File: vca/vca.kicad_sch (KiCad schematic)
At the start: 22 parts, among them U4 STM32F103C6Tx, Y1 Crystal_8Mhz

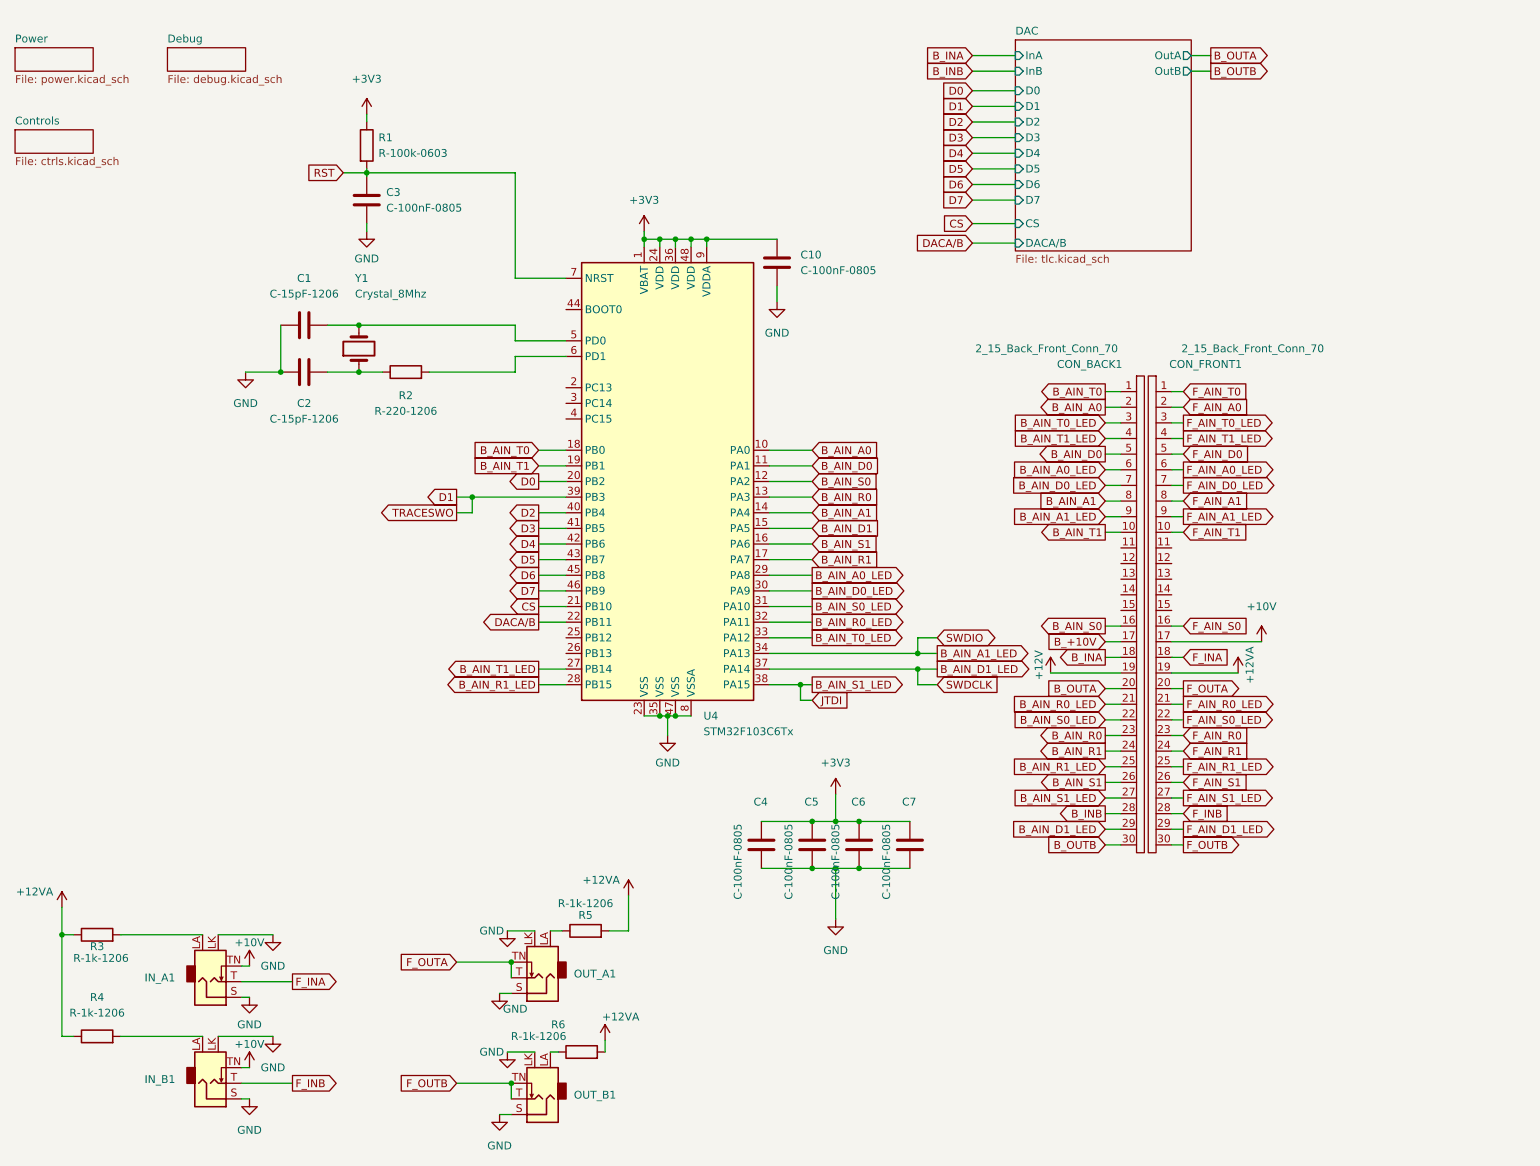
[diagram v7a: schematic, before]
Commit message: Fixed some pins on the connectors, and working on the back board, power left to go
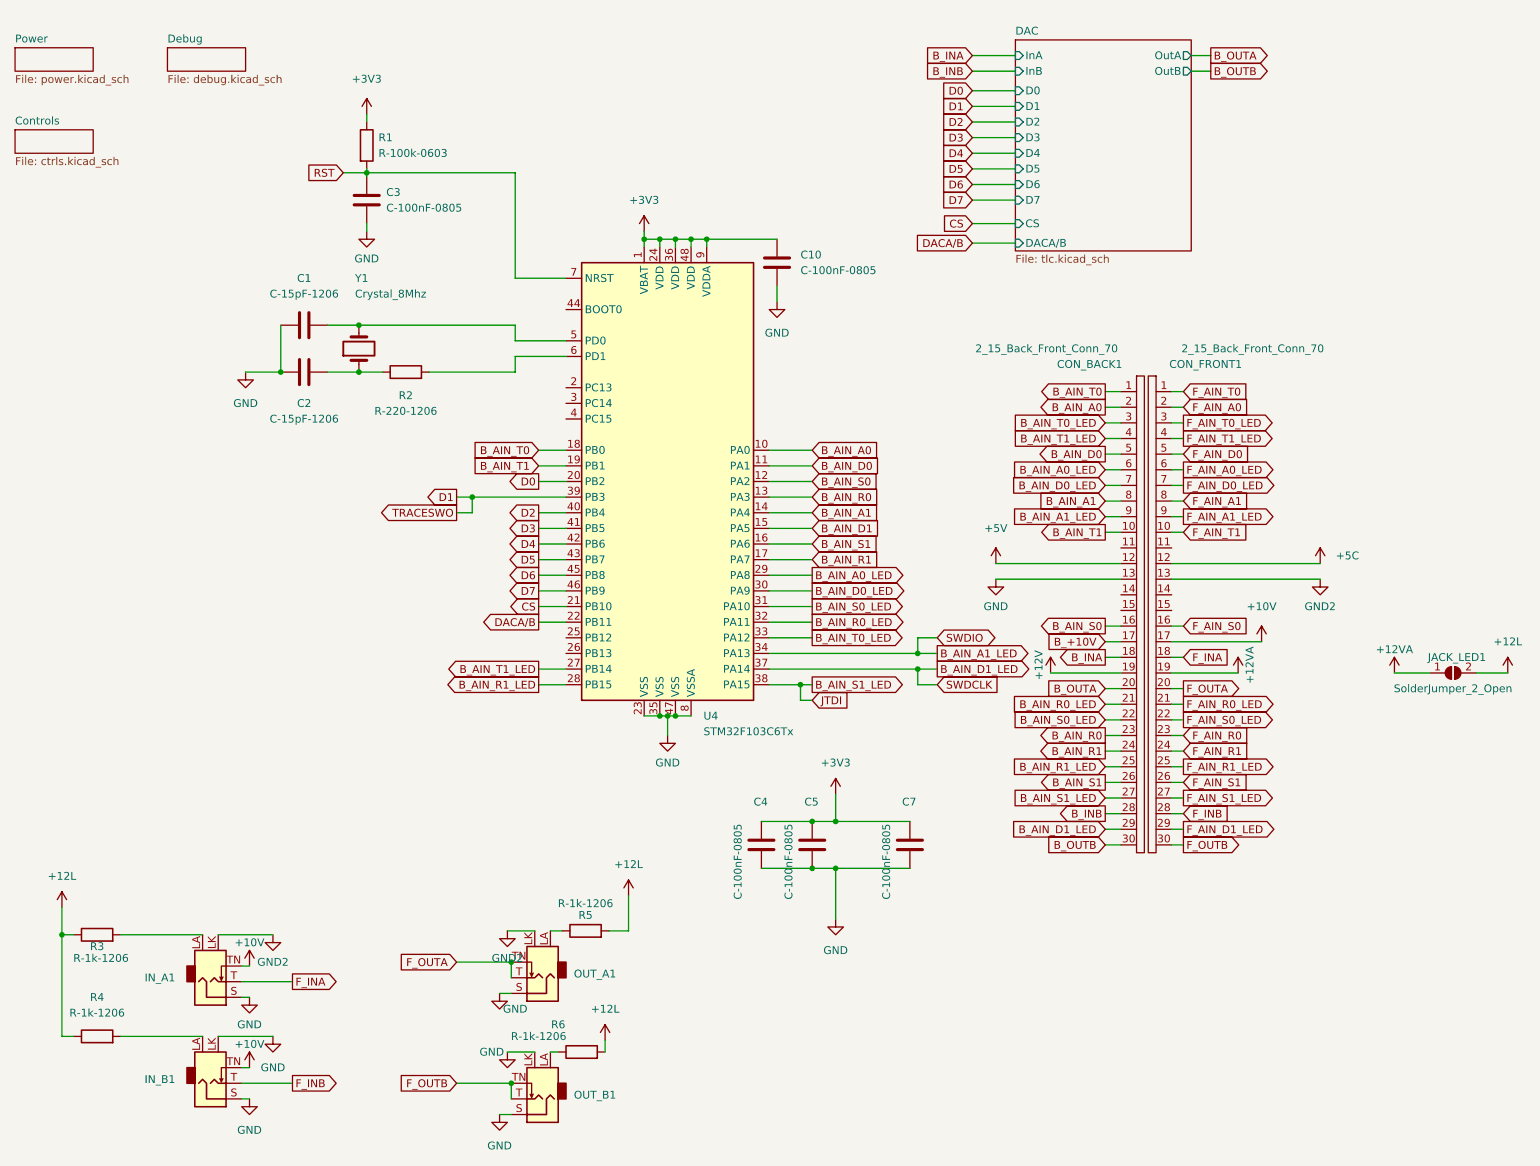
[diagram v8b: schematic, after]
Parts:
- removed C6: C-100nF-0805, Capacitor_SMD:C_0805_2012Metric_Pad1.18x1.45mm_HandSolder, symbol eurorack:C-100nF-0805
- added JACK_LED1: SolderJumper_2_Open, Jumper:SolderJumper-2_P1.3mm_Open_Pad1.0x1.5mm, symbol Jumper:SolderJumper_2_Open
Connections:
- net +12VA: now also JACK_LED1.1 (A); no longer R3.1, R4.1, R5.2, R6.2
- net GND: now also CON_BACK1.13; no longer IN_A1.LK, OUT_A1.LK
- net +5V: now reaches CON_BACK1.12
- net +5C: now reaches CON_FRONT1.12
- net GND2: now reaches CON_FRONT1.13
- net GND2: now also IN_A1.LK, OUT_A1.LK
- new net +12L: JACK_LED1.2 (B), R3.1, R4.1, R5.2, R6.2
